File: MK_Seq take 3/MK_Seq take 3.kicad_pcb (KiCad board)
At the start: 2 copper layers, 90 x 100 mm, 123 parts, among them J1 IDC 2x5, Q1 2N3904, Q2 2N3904, Q3 2N3904, Q4 2N3904, Q5 2N3904, Q6 2N3904, Q7 2N3904, Q8 2N3904, Q9 BC548, SW9 SW_Push_SPDT, Sw1 SP,DT, Sw2 SP,DT, Sw3 SP,DT, Sw4 SP,DT, Sw5 SP,DT, Sw6 SP,DT, Sw7 SP,DT, Sw8 SP,DT, T1 10K, T2 2K, U1 4017, U2 TL074

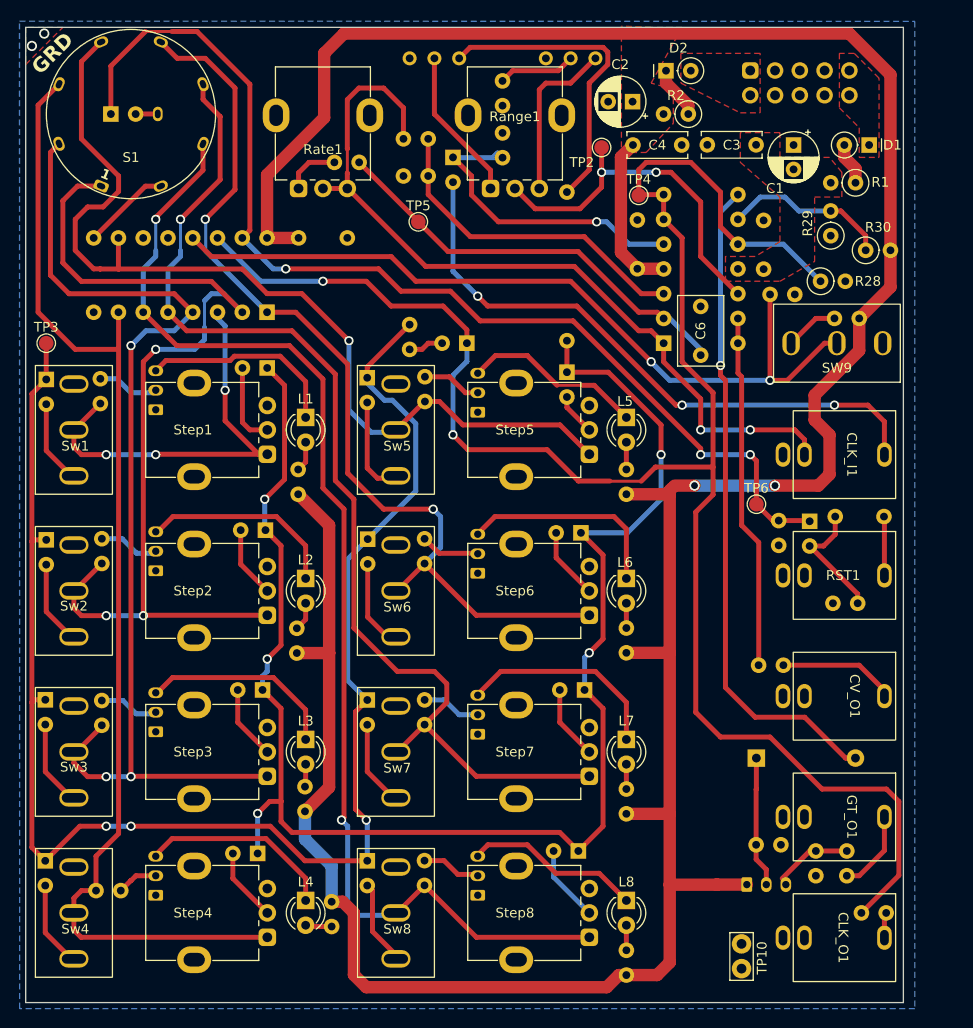
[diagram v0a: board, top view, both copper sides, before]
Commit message: PCB design from scratch now.
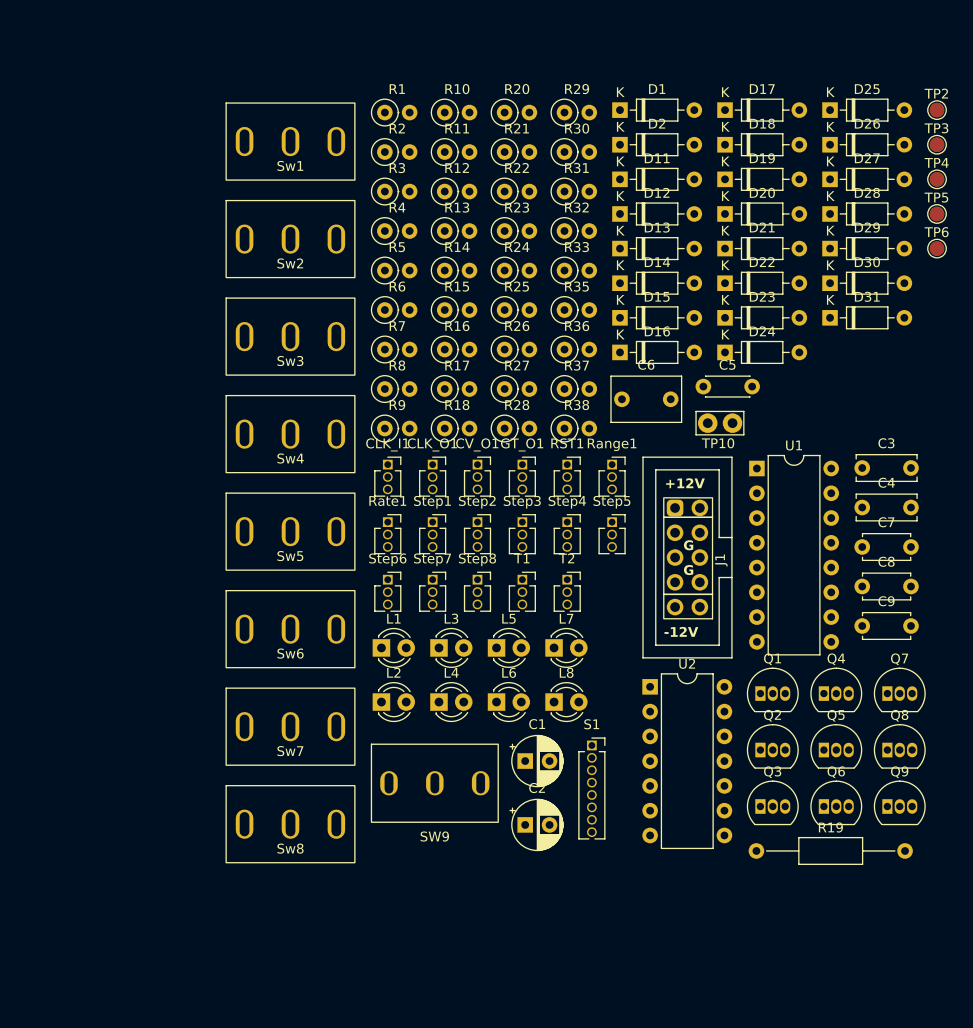
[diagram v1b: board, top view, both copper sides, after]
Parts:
- removed G***: LOGO, My_Library:Homonculus Graphic.kicad_10mm_mod
- C5, C7, C8, C9, J1, R10, R11, R12, R13, R14, R15, R16, R17, R18, R19, R20, R21, R22, R23, R24, R25, R26, R27, R3, R31, R32, R33, R35, R36, R37, R38, R4, R5, R6, R7, R8, R9, U1, U2: moved to F.Cu
- CLK_I1, CLK_O1, CV_O1, GT_O1, RST1: footprint My_Library:Connector 3.5mm Mono Switched -> Connector_PinSocket_1.27mm:PinSocket_1x03_P1.27mm_Vertical
- D1, D2: footprint My_Library:Diode_THT_P2.54mm_Vertical_KathodeUp -> Diode_THT:D_DO-35_SOD27_P7.62mm_Horizontal
- D11, D12, D13, D14, D15, D16, D17, D18, D19, D20, D21, D22, D23, D24, D25, D26, D27, D28, D29, D30: footprint My_Library:Diode_THT_P2.54mm_Vertical_KathodeUp -> Diode_THT:D_DO-35_SOD27_P7.62mm_Horizontal; moved to F.Cu
- D31: footprint Diode_THT:D_A-405_P10.16mm_Horizontal -> Diode_THT:D_DO-35_SOD27_P7.62mm_Horizontal; moved to F.Cu
- Q1, Q2, Q3, Q4, Q5, Q6, Q7, Q8: footprint My_Library:Transistor_TL092_Inline_Cut Silk -> Package_TO_SOT_THT:TO-92_Inline; moved to F.Cu
- Q9: footprint My_Library:Transistor_TL092_Inline -> Package_TO_SOT_THT:TO-92_Inline; moved to F.Cu
- Range1, Rate1, Step1, Step2, Step3, Step4, Step5, Step6, Step7, Step8: footprint My_Library:Potentiometer_Alpha_RD901F-40-00D_Single_Vertical -> Connector_PinSocket_1.27mm:PinSocket_1x03_P1.27mm_Vertical
- S1: footprint My_Library:Rotary Switch, 1 Pole, 8 Positions -> Connector_PinSocket_1.27mm:PinSocket_1x08_P1.27mm_Vertical
- T1, T2: footprint Potentiometer_THT:Potentiometer_Bourns_3296W_Vertical -> Connector_PinSocket_1.27mm:PinSocket_1x03_P1.27mm_Vertical; moved to F.Cu
- moved D26 108.9 mm to (102.2, 31.7), turned to 0 degrees
- moved D27 96.6 mm to (102.2, 35.3), turned to 0 degrees
- moved TP3 93.6 mm to (113.1, 31.7)
- moved R10 87.4 mm to (62.7, 28.4)
- moved D28 87.0 mm to (102.2, 38.8), turned to 0 degrees
- moved D29 81.5 mm to (102.2, 42.4), turned to 0 degrees
- moved C2 75.0 mm to (70.9, 101.5), turned to 0 degrees
- moved R14 74.6 mm to (62.7, 44.6), turned to 0 degrees
- moved S1 74.1 mm to (77.7, 93.3)
- moved D18 74.0 mm to (91.4, 31.7), turned to 0 degrees
- moved R33 72.6 mm to (74.9, 44.6)
- moved Q4 71.4 mm to (101.5, 88.0), turned to 0 degrees
- moved R32 71.0 mm to (74.9, 40.6), turned to 0 degrees
- moved SW9 70.4 mm to (61.6, 103.2), turned to 0 degrees
- moved R31 69.8 mm to (74.9, 36.5)
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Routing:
- net +12V: track 324.7 -> 0.00 mm, vias 2 -> 0
- net Clock: track 195.4 -> 0.00 mm, vias 2 -> 0
- net Steps_CV_Out: track 157.6 -> 0.00 mm, vias 5 -> 0
- net Steps_Trig_Out: track 156.9 -> 0.00 mm, vias 3 -> 0
- net Step8: track 125.0 -> 0.00 mm, vias 2 -> 0
- net Step4: track 120.4 -> 0.00 mm
- net Step7: track 113.2 -> 0.00 mm, vias 1 -> 0
- net Reset: track 112.1 -> 0.00 mm, vias 3 -> 0
- net Step3: track 107.3 -> 0.00 mm, vias 3 -> 0
- net Step2: track 99.3 -> 0.00 mm, vias 3 -> 0
- net Step6: track 98.2 -> 0.00 mm, vias 2 -> 0
- net Step5: track 97.8 -> 0.00 mm, vias 1 -> 0
- net Net-(CLK_I1-TN): track 83.9 -> 0.00 mm, vias 2 -> 0
- net Net-(SW9-B): track 82.5 -> 0.00 mm, vias 2 -> 0
- net Net-(D31-A): track 67.8 -> 0.00 mm, vias 1 -> 0
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- removed copper zone on F.Cu, net +12V
- removed copper zone on F.Cu, net -12V
- removed copper zone on F.Cu, net /+12IN
- removed copper zone on F.Cu, net /-12IN
- removed copper zone on B.Cu, net Earth
- removed copper zone on F.Cu, net Earth
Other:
- board outline removed
- board text removed: "GRD"
- board text removed: "MK8-Homunculus Seq PCB v1.11 G. Robison 8/4/2024"

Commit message: Working on Seq Rev 3.
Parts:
- added J2: Conn_01x10_Pin, Connector_PinHeader_2.54mm:PinHeader_1x10_P2.54mm_Vertical, F.Cu at (297.2, 52.2)
- added J3: Conn_01x10_Pin, Connector_PinSocket_2.54mm:PinSocket_1x10_P2.54mm_Vertical, F.Cu at (301.9, 52.2)
- S1: footprint Connector_PinSocket_1.27mm:PinSocket_1x08_P1.27mm_Vertical -> My_Library:Rotary Switch, 1 Pole, 8 Positions
- Step1, Step2, Step3, Step4, Step5, Step6, Step7, Step8: footprint Connector_PinSocket_1.27mm:PinSocket_1x03_P1.27mm_Vertical -> My_Library:Potentiometer_Alpha_RD901F-40-00D_Single_Vertical
- moved C5 163.1 mm to (252.0, 47.1)
- moved C6 163.1 mm to (243.6, 48.4)
- moved D17 163.1 mm to (254.2, 18.8)
- moved D18 163.1 mm to (254.2, 22.3)
- moved D19 163.1 mm to (254.2, 25.9)
- moved D20 163.1 mm to (254.2, 29.4)
- moved D21 163.1 mm to (254.2, 33.0)
- moved D22 163.1 mm to (254.2, 36.5)
- moved D23 163.1 mm to (254.2, 40.1)
- moved D24 163.1 mm to (254.2, 43.6)
- moved J1 163.1 mm to (249.9, 59.6)
- moved L1 163.1 mm to (219.0, 73.9)
- moved L2 163.1 mm to (219.0, 79.5)
- moved L7 163.1 mm to (236.7, 73.9)
- moved L8 163.1 mm to (236.7, 79.5)
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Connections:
- net Step9 renamed EOC
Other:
- board outline added: 99.1 x 99.1 mm
